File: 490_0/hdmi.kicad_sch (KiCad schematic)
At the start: 8 parts, among them J19 467650301, U10 EMI8142MUTAG, U9 EMI8142MUTAG

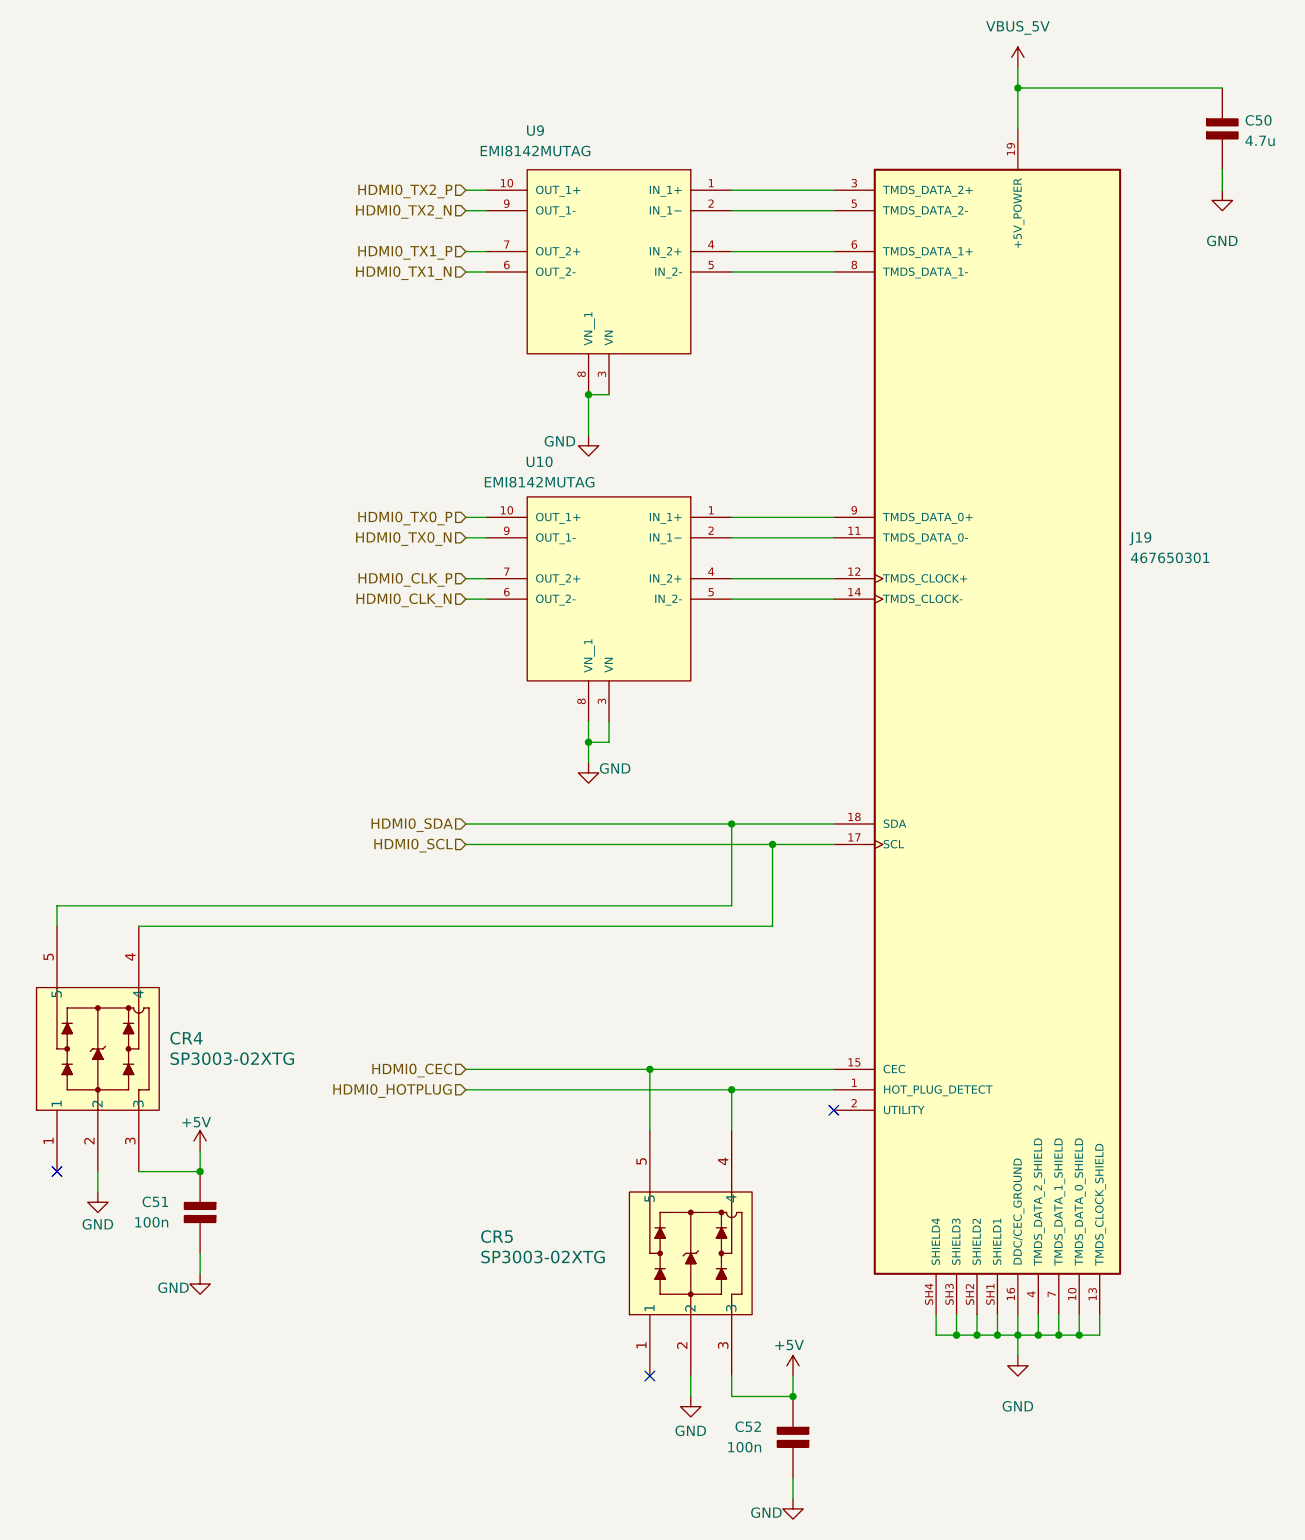
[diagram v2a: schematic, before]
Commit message: Implemented suggestions
notes on schematics:
Overall: Schematics needs to be improved, more compact and cleaner
=========================
I) on root page (page 1):
overall: needs a bit of clean up of the diagram

1. the diagram shows pcb3 and pcb1, but no pcb2, it is probably outdated and therefore might have errors in it, fix it to the latest version and rename things to reflect what it actually is. Also try to clean it up a bit
2. The PCB-3 seem to have the cameras directly connected to the usb hub, how will this be connected? with connectors? if so add them to the diagram, if it's with wires soldered directly to the pcb, try to make note of it for clarity
4. for some reason your TOF is above PCB-3 but is only connected to PCB1, will the TOF be on the glasses, or will you be moving this to the main board? maybe have TOF on the chest for depth, and 2 cameras on glasses for vision, it will also reduce length of cable, which is ideal, i don't think it will work if you run it from the glasses to pcb1 though.
I know, this is a problem, we discussed the chest thing, the problem is the length of the cable but also the haptic feedback is weird if they turn their head.
5. Rename PCB1/PCB3 to PCB1 (chest) PCB3 (glasses) for clarity. Also i don't think (mayeb i'm wrong) that the 5 conected buttons should be on a bus, a bus implies that multiple devices communicate on the same single line. You're using individual lines for each to individual gpio, no?

=========================
II) on PCB-3 usb 2.0 bridge page (page 10)
overall: check datasheet and make sure you've done the connection right and values are selected properly, with the chip data lines properly pulled up/down whether externally or internally. This is important

1. C3/C11 are the input capacitors to U2/u3 TPS553DBVR, datasheet says 100nF, you used 10uF, why? stick to 100nF
2. you seem to have implemented one of /Uthe typical application circuit, look at the others. You have on page 21 of datasheet an auto-retry wi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
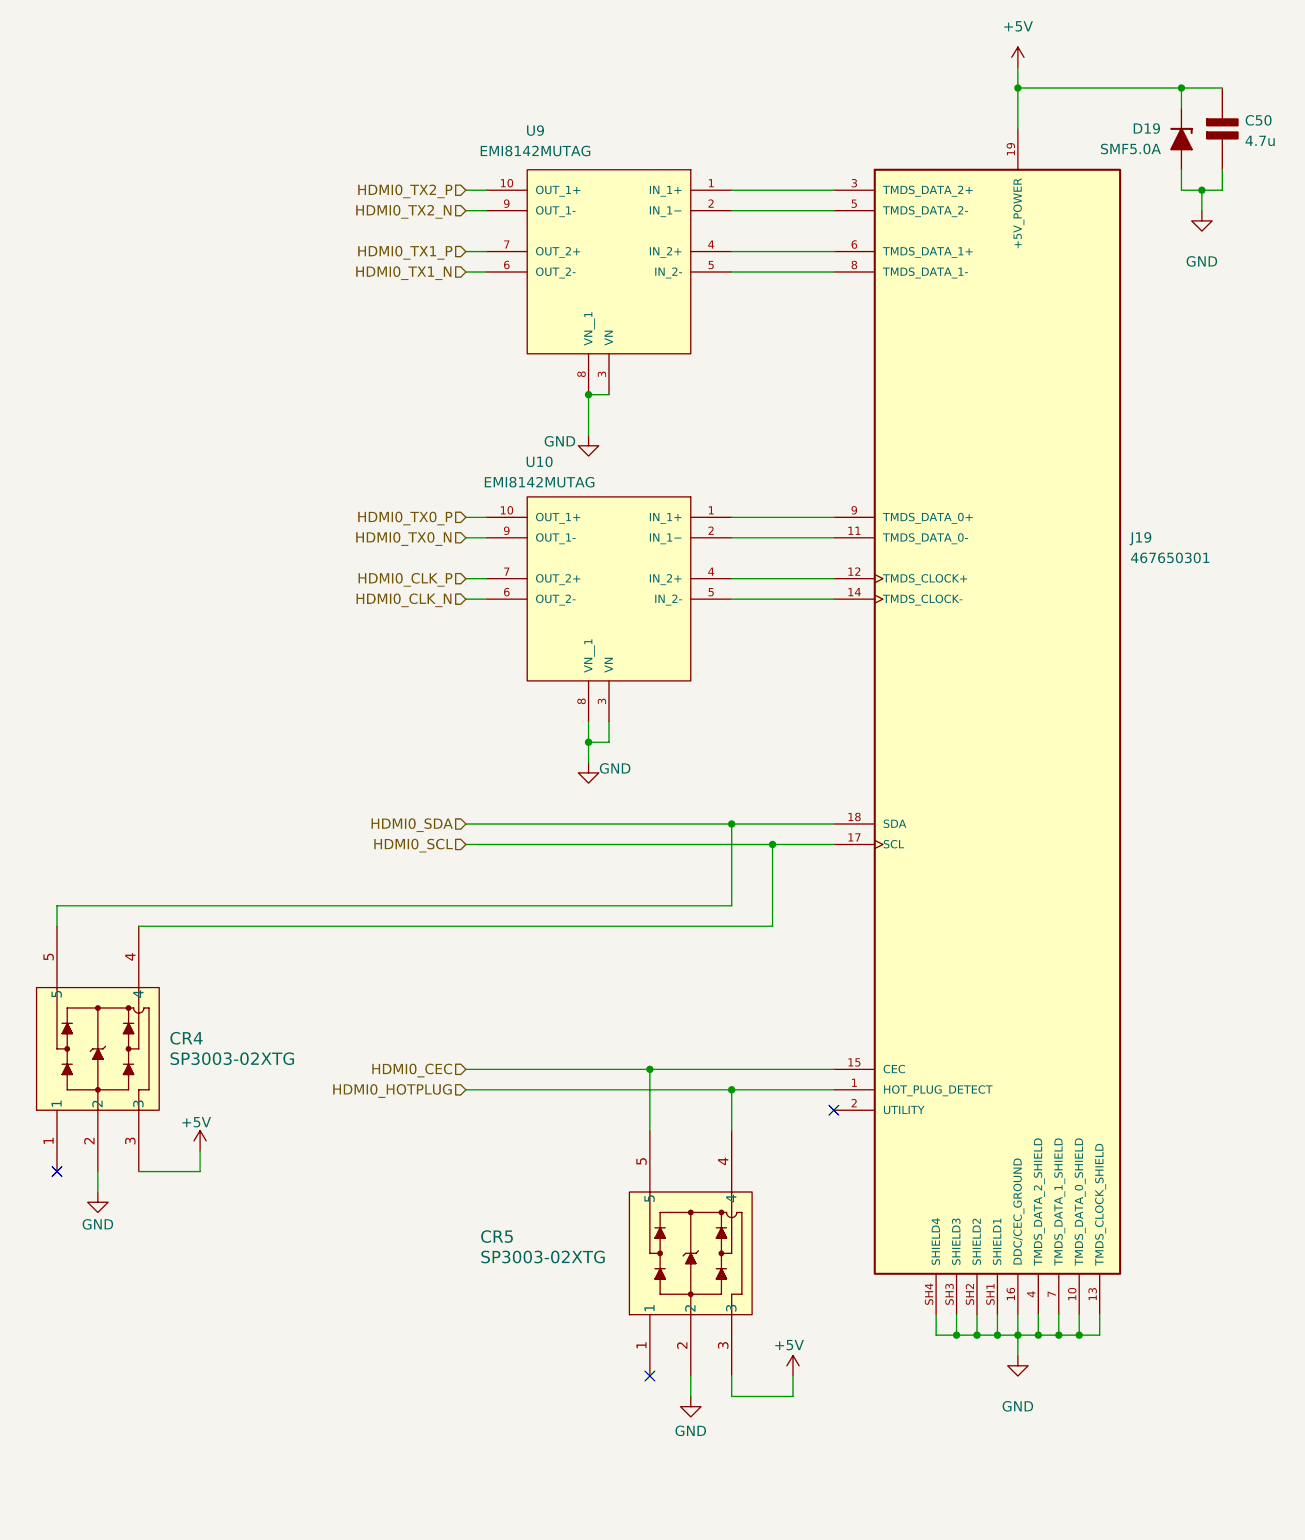
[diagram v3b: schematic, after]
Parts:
- removed C51, C52: 100n, symbol PCM_Elektuur:C
- added D19: SMF5.0A, PCM_Diode_SMD_AKL:D_SOD-123F, symbol PCM_Diode_TVS_AKL:SMF5.0A
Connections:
- net VBUS_5V is gone; now on net +5V: C50.1 (+), J19.19 (+5V_POWER)
- net +5V: now also D19.1 (K)
- net GND: now also D19.2 (A)

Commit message: Footprint Update
1st half of footprints updated
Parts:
- CR4, CR5: footprint (none) -> *CapStone*:SOT553_LTF_SP3003_02XTG
- D19: footprint PCM_Diode_SMD_AKL:D_SOD-123F -> Diode_SMD:D_SOD-123F
- J19: footprint 467650301:MOLEX_467650301 -> *CapStone*:MOLEX_467650301
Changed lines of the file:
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@@
 			)
 		)
-		(property "Footprint" ""
+		(property "Footprint" "*CapStone*:SOT553_LTF_SP3003_02XTG"
 			(at 20.32 157.48 0)
 			(effects
@@
 			)
 		)
-		(property "Footprint" "467650301:MOLEX_467650301"
+		(property "Footprint" "*CapStone*:MOLEX_467650301"
 			(at 149.86 55.88 0)
 			(effects
@@
 			)
 		)
-		(property "Footprint" ""
+		(property "Footprint" "*CapStone*:SOT553_LTF_SP3003_02XTG"
 			(at 93.98 182.88 0)
 			(effects
@@
 			)
 		)
-		(property "Footprint" "PCM_Diode_SMD_AKL:D_SOD-123F"
+		(property "Footprint" "Diode_SMD:D_SOD-123F"
 			(at 160.02 29.21 0)
 			(effects

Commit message: Footprint Update #2
All footprints except for the capacitors have been attributed
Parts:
- U10: footprint (none) -> *CapStone*:SON40P220X135X50-10N_EMI8142MUTAG
- U9: footprint EMI8142MUTAG:SON40P220X135X50-10N -> *CapStone*:SON40P220X135X50-10N_EMI8142MUTAG
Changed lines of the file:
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@@
 			)
 		)
-		(property "Footprint" "EMI8142MUTAG:SON40P220X135X50-10N"
+		(property "Footprint" "*CapStone*:SON40P220X135X50-10N_EMI8142MUTAG"
 			(at 88.9 43.18 0)
 			(effects
@@
 			)
 		)
-		(property "Footprint" ""
+		(property "Footprint" "*CapStone*:SON40P220X135X50-10N_EMI8142MUTAG"
 			(at 88.9 83.82 0)
 			(effects

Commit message: March 3rd
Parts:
- removed D19: SMF5.0A, Diode_SMD:D_SOD-123F, symbol PCM_Diode_TVS_AKL:SMF5.0A
- C50: footprint (none) -> Capacitor_SMD:C_0603_1608Metric; Digikey Link https://www.digikey.ca/en/products/detail/kemet/c1206c475k8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 -> https://www.digikey.ca/en/products/detail/murata-electronic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; Manufacturer KEMET -> Murata Electronics; Manufacturer Part C1206C475K8RACTU -> GRM188Z71A475KE15D; Package 1206 (3216 Metric) -> 0603 (1608 Metric); Price 0.51 -> 0.22; Supplier P/N 399-C1206C475K8RACTUCT-ND -> 490-GRM188Z71A475KE15DCT-ND; Type SMD -> SMD, MLCC
- renumbered CR4 to U13, CR5 to U14
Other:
- moved on the sheet: C50, J19, U10, U13, U14, U9

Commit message: Added side B for SW1
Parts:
- C50: symbol PCM_Elektuur:C -> capstone_parts:C
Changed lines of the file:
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@@
 	)
 	(symbol
-		(lib_id "PCM_Elektuur:C")
+		(lib_id "capstone_parts:C")
 		(at 162.56 22.86 0)
 		(mirror y)

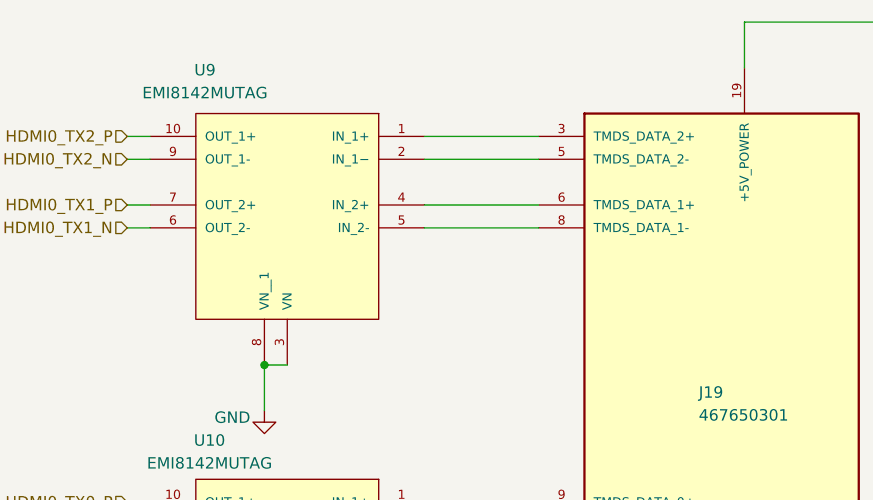
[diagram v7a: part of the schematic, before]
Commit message: started routing up to HDMI ESD impedance matching
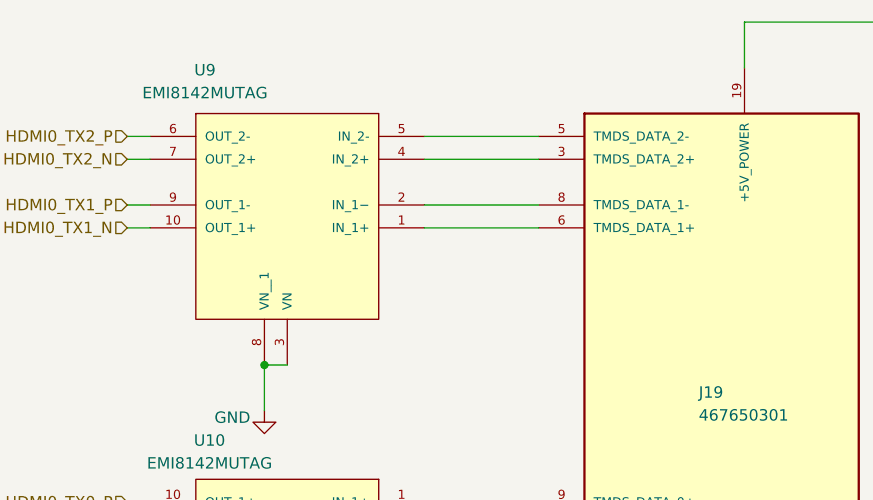
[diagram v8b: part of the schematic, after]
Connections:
- net HDMI0_TX1_N: now also U9.10 (OUT_1+); no longer U9.6 (OUT_2-)
- net HDMI0_TX1_P: now also U9.9 (OUT_1-); no longer U9.7 (OUT_2+)
- net HDMI0_TX2_N: now also U9.7 (OUT_2+); no longer U9.9 (OUT_1-)
- net HDMI0_TX2_P: now also U9.6 (OUT_2-); no longer U9.10 (OUT_1+)
- net at J19.3 (TMDS_DATA_2+): now also U9.4 (IN_2+); no longer U9.1 (IN_1+)
- net at J19.5 (TMDS_DATA_2-): now also U9.5 (IN_2-); no longer U9.2 (IN_1−)
- net at J19.6 (TMDS_DATA_1+): now also U9.1 (IN_1+); no longer U9.4 (IN_2+)
- net at J19.8 (TMDS_DATA_1-): now also U9.2 (IN_1−); no longer U9.5 (IN_2-)
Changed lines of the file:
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@@
 	)
 	(symbol
+		(lib_name "EMI8142MUTAG_1")
 		(lib_id "capstone_parts:EMI8142MUTAG")
 		(at 86.36 38.1 0)
